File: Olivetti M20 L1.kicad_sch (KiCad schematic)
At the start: 0 parts

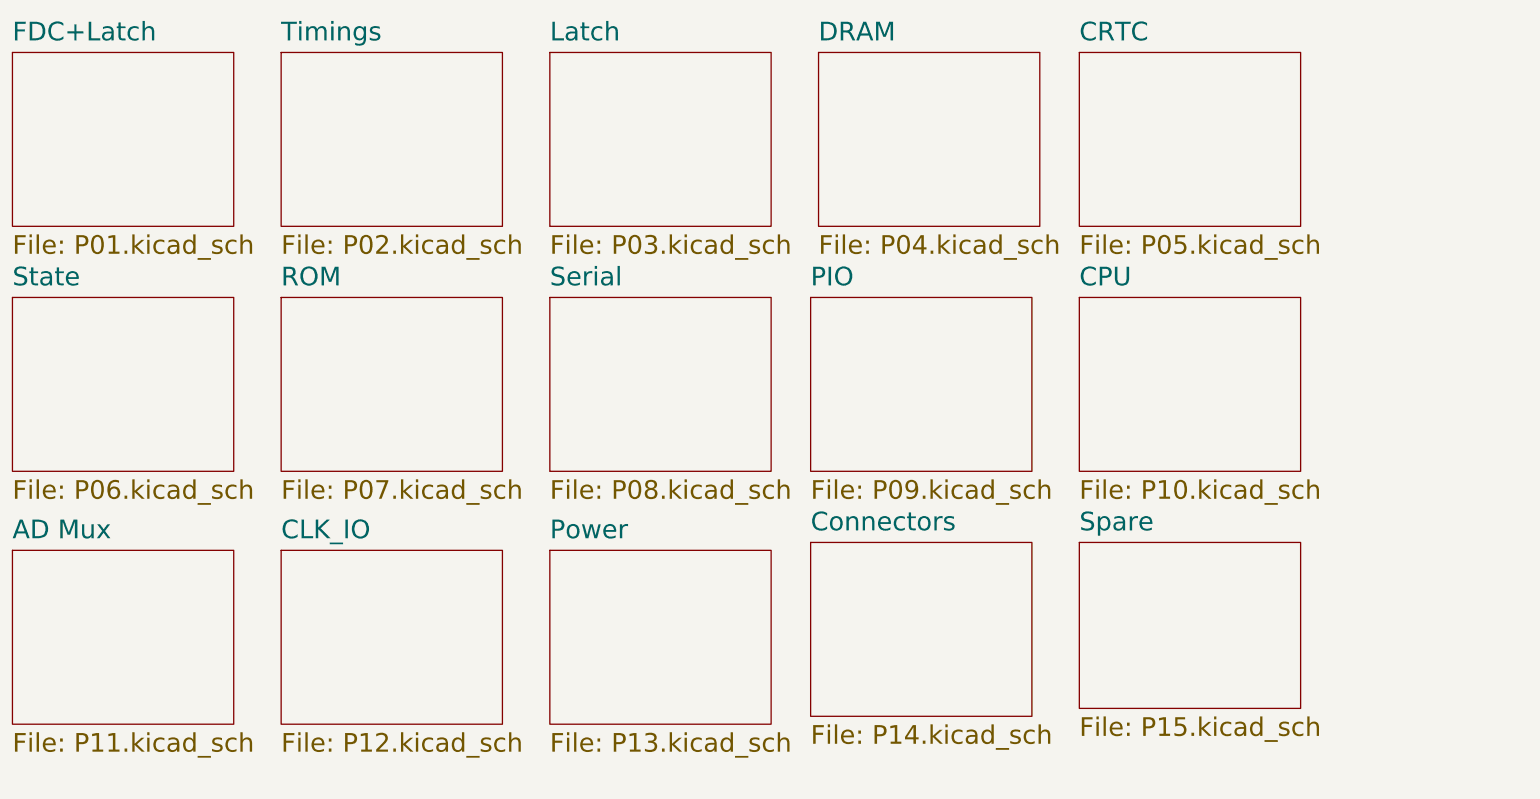
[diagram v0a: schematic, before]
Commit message: fixing KiCad6 warnings
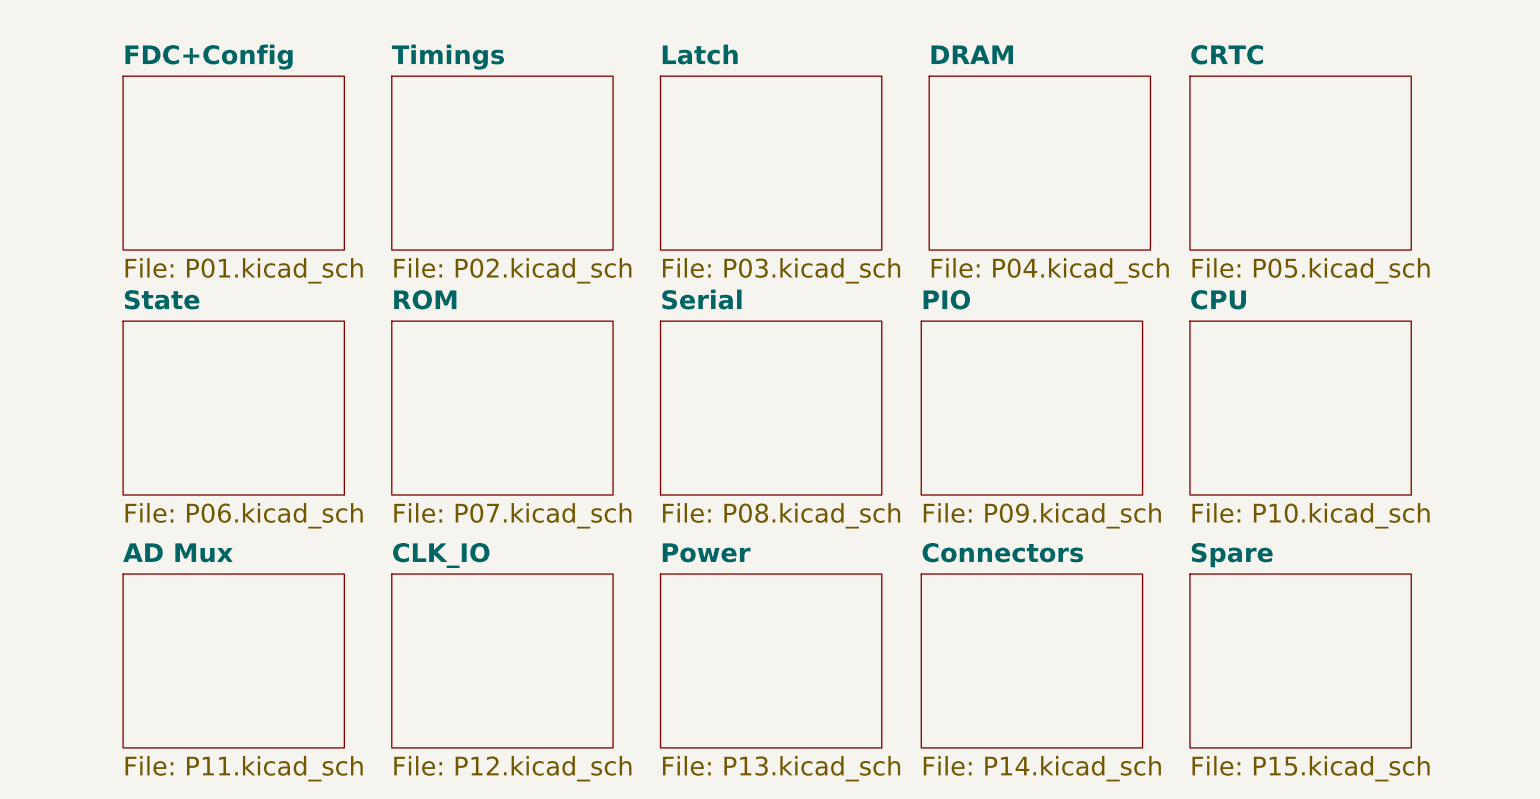
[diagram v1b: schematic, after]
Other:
- sheet FDC+Latch renamed FDC+Config
